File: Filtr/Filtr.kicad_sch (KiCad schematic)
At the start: 38 parts, among them J1 Jack-DC, J2 Conn_01x04_Pin, SW3 RotaryEncoder_Switch, U1 TPS562200, U2 STM32G030K6Tx

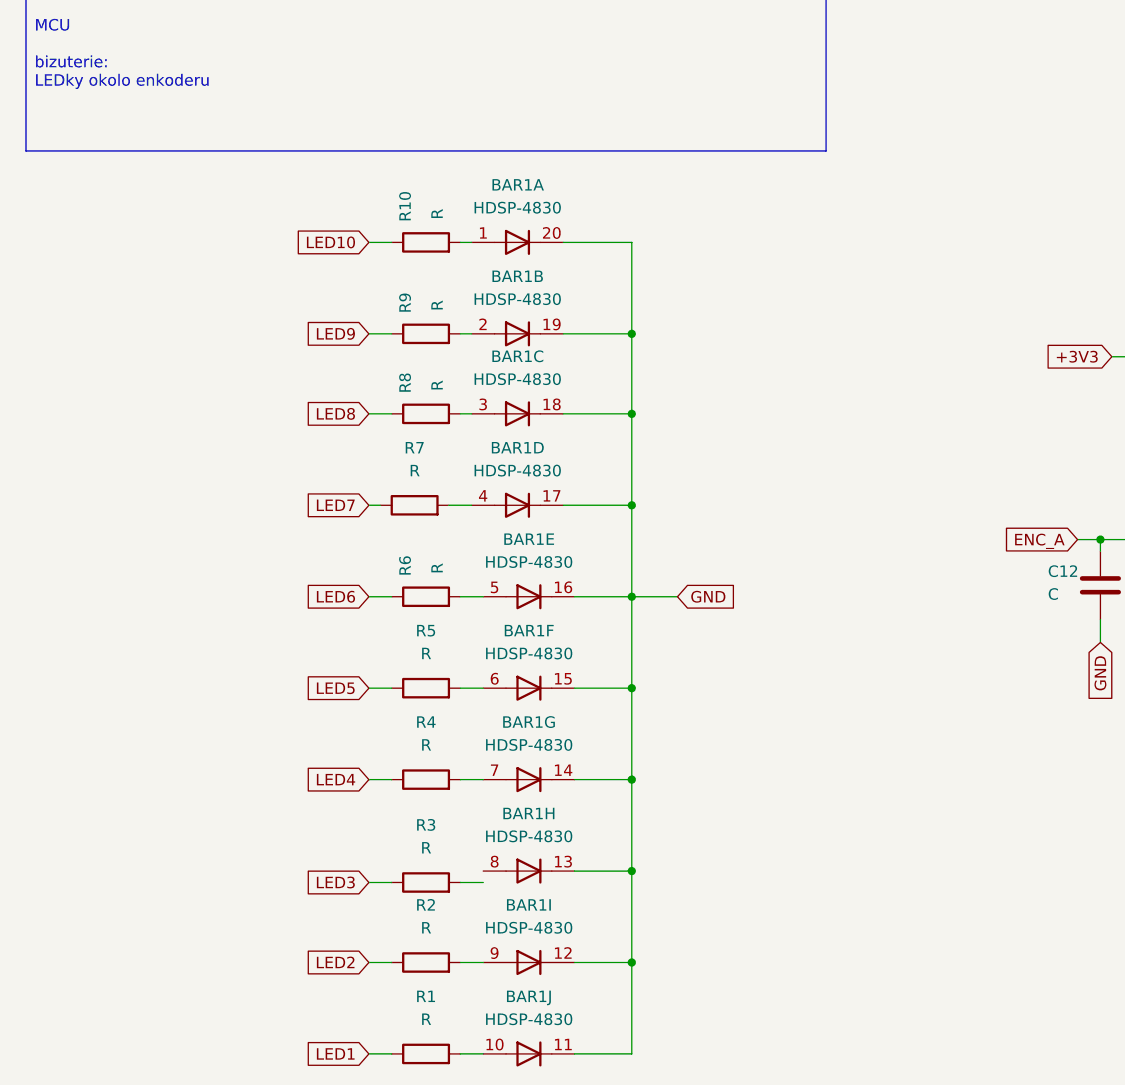
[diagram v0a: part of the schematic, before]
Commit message: Vymazani CubeIDE
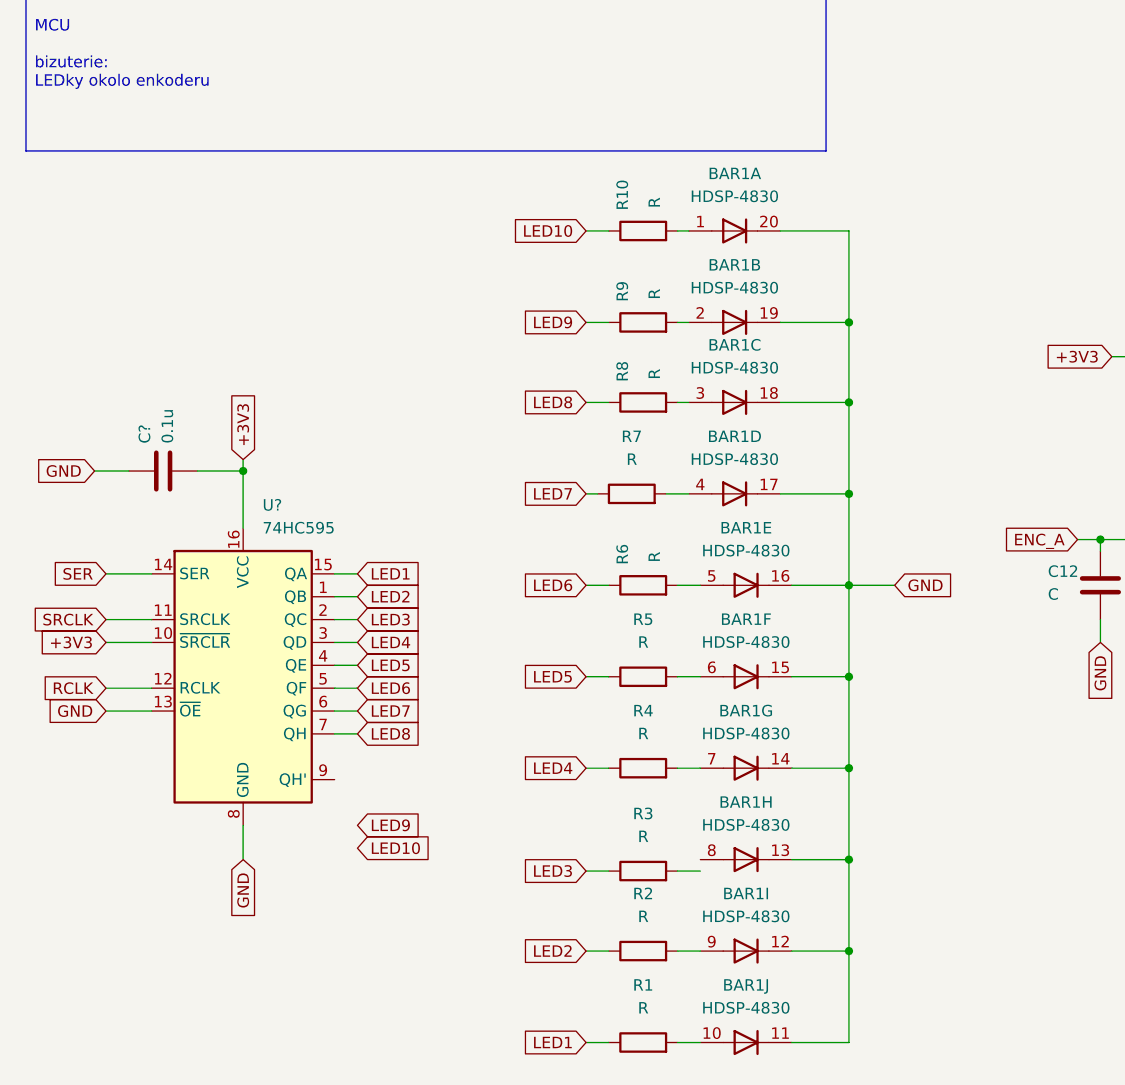
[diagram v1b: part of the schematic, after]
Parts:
- added C?: 0.1u, Capacitor_SMD:C_0603_1608Metric, symbol Device:C
- added U?: 74HC595, symbol 74xx:74HC595
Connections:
- net +3V3: now also C?.1, U?.10 (~{SRCLR}), U?.16 (VCC)
- net GND: now also C?.2, U?.13 (~{OE}), U?.8 (GND)
- net LED1: now also U?.15 (QA)
- net LED2: now also U?.1 (QB)
- net LED3: now also U?.2 (QC)
- net LED4: now also U?.3 (QD)
- net LED5: now also U?.4 (QE)
- net LED6: now also U?.5 (QF)
- net LED7: now also U?.6 (QG)
- net LED8: now also U?.7 (QH)
- new net RCLK: U?.12 (RCLK)
- new net SER: U?.14 (SER)
- new net SRCLK: U?.11 (SRCLK)
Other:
- moved on the sheet: BAR1A, BAR1B, BAR1C, BAR1D, BAR1E, BAR1F, BAR1G, BAR1H, BAR1I, BAR1J, R1, R10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

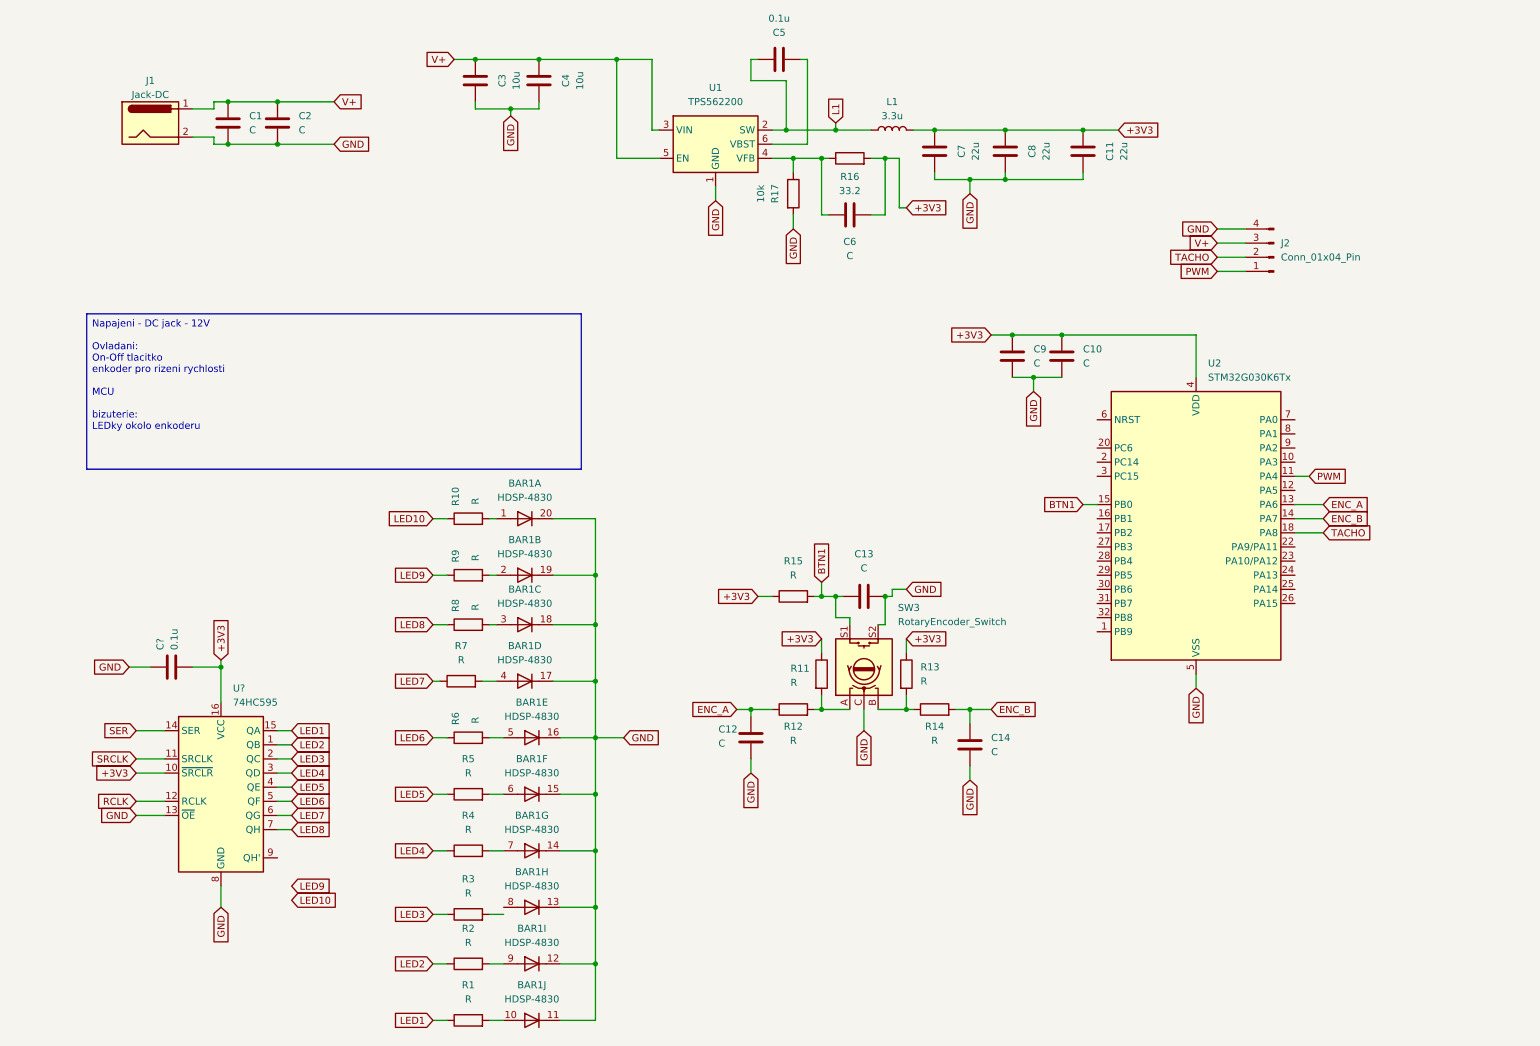
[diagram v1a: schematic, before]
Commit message: CubeIDE a Kicad
CubeIDE -nastaveni pinu
Kicad - pridani shift registru
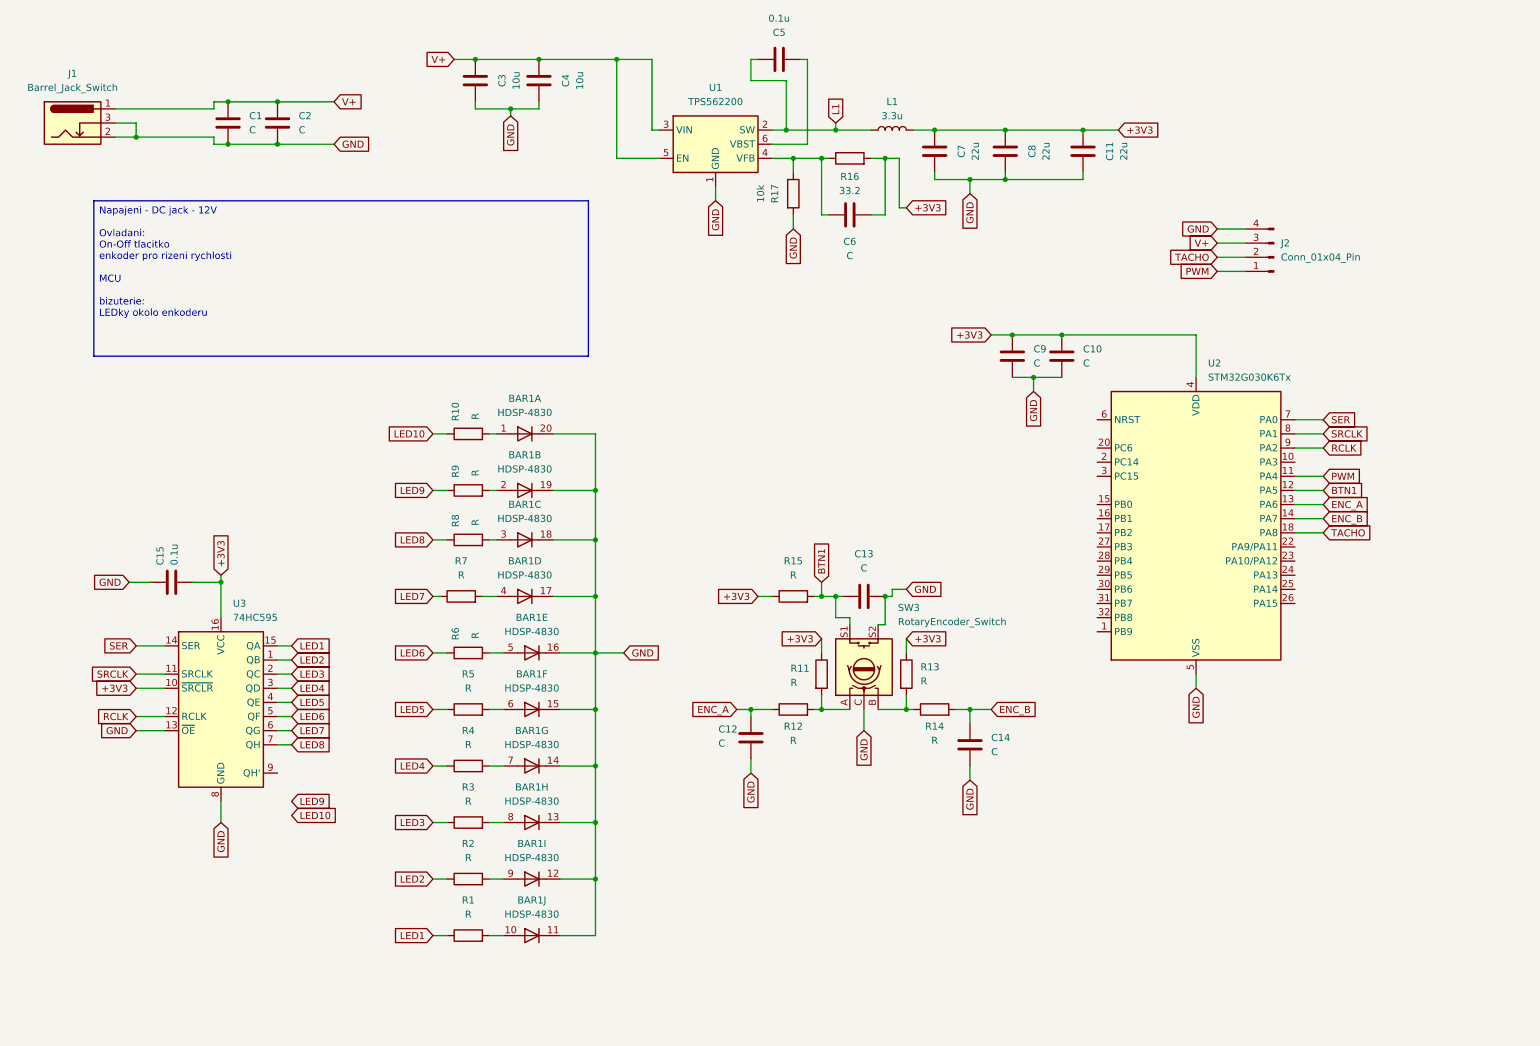
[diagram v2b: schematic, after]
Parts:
- removed J1: Jack-DC, Connector_BarrelJack:BarrelJack_CLIFF_FC681465S_SMT_Horizontal, symbol Connector:Jack-DC
- added J1: Barrel_Jack_Switch, Connector_BarrelJack:BarrelJack_CLIFF_FC681465S_SMT_Horizontal, symbol Connector:Barrel_Jack_Switch
- U3: renamed from U?; footprint (none) -> Package_SO:SO-16_5.3x10.2mm_P1.27mm
- gave numbers to parts that had none: 1
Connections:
- net BTN1: now also U2.12 (PA5); no longer U2.15 (PB0)
- net GND: now also J1.2, J1.3
- net RCLK: now also U2.9 (PA2)
- net SER: now also U2.7 (PA0)
- net SRCLK: now also U2.8 (PA1)
- net V+: now also J1.1
- net at BAR1.8 (A): now also R3.2
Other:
- moved on the sheet: BAR1A, BAR1B, BAR1C, BAR1D, BAR1E, BAR1F, BAR1G, BAR1H, BAR1I, BAR1J, C15, R1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

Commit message: Novy Design desky
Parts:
- removed BAR1: HDSP-4830, Display:HDSP-4830, symbol LED:HDSP-4830
- removed C15: 0.1u, Capacitor_SMD:C_0603_1608Metric, symbol Device:C
- removed C2: C, Capacitor_THT:CP_Radial_D10.0mm_P5.00mm, symbol Device:C
- removed C6: C, Capacitor_SMD:C_1206_3216Metric, symbol Device:C
- removed R10, R7, R8, R9: R, Resistor_SMD:R_0603_1608Metric, symbol Device:R
- removed U3: 74HC595, Package_SO:SO-16_5.3x10.2mm_P1.27mm, symbol 74xx:74HC595
- added H1, H2, H3, H4: MountingHole_Pad, MountingHole:MountingHole_3.2mm_M3_DIN965_Pad, symbol Mechanical:MountingHole_Pad
- added J2: Conn_02x05_Odd_Even, Connector_PinHeader_2.54mm:PinHeader_2x05_P2.54mm_Vertical, symbol Connector_Generic:Conn_02x05_Odd_Even
- added ProgConn1: Conn_01x04_Pin, Connector_PinHeader_2.54mm:PinHeader_1x04_P2.54mm_Vertical, symbol Connector:Conn_01x04_Pin
- R6: footprint Resistor_SMD:R_0603_1608Metric -> Resistor_SMD:R_1206_3216Metric
- renumbered J2 to Fan1
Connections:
- net LED6 is gone; now on net +3V3: R6.1
- net +3V3: now also ProgConn1.4 (Pin_4)
- net GND: now also H1.1, H2.1, H3.1, H4.1, J2.10 (Pin_10), J2.2 (Pin_2), J2.4 (Pin_4), J2.6 (Pin_6), J2.8 (Pin_8), ProgConn1.3 (Pin_3)
- net LED1: now also U2.27 (PB3)
- net LED2: now also U2.28 (PB4)
- net LED3: now also U2.29 (PB5)
- net LED4: now also U2.30 (PB6)
- net LED5: now also U2.31 (PB7)
- net PWM: now also U2.16 (PB1); no longer U2.11 (PA4)
- net TACHO: now also R6.2
- net at R1.2: now also J2.9 (Pin_9)
- net at R4.2: now also J2.3 (Pin_3)
- net at R5.2: now also J2.1 (Pin_1)
- net at R2.2: now also J2.7 (Pin_7)
- net at R3.2: now also J2.5 (Pin_5)
- net SWDIO: now reaches U2.24 (PA13)
- net SWDIO: now also ProgConn1.2 (Pin_2)
- net SWCLK: now reaches U2.25 (PA14)
- net SWCLK: now also ProgConn1.1 (Pin_1)
- net RCLK: no longer names the net of U2.9 (PA2)
- net SER: no longer names the net of U2.7 (PA0)
- net SRCLK: no longer names the net of U2.8 (PA1)
